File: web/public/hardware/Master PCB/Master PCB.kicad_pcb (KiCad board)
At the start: 2 copper layers, 100 x 100 mm, 98 parts, among them J1 Rows 0-15, J10 LDR2, J11 LDR3, J12 LDR4, J13 SWD Conn, J14 LED Conn, J15 OLED1, J16 OLED2, J17 Relay Conn, J2 Cols 0-21, J3 Cols 22-31, J4 5V_IN, J5 LED1, J6 LED2, J7 LED3, J8 LED4, J9 LDR1, Q1 2N7000, Q2 2N7000, Q3 2N7000, Q4 2N7000, SW1 nRST, SW2 Menu Encoder, U1 STM32U585VITx, U2 M95P32-IXMNT, U3 TLV62568DBV, U4 LM339, U5 MAX7375AXR805, U6 USBLC6-4SC6, U7 USBLC6-2SC6, U8 USBLC6-2SC6

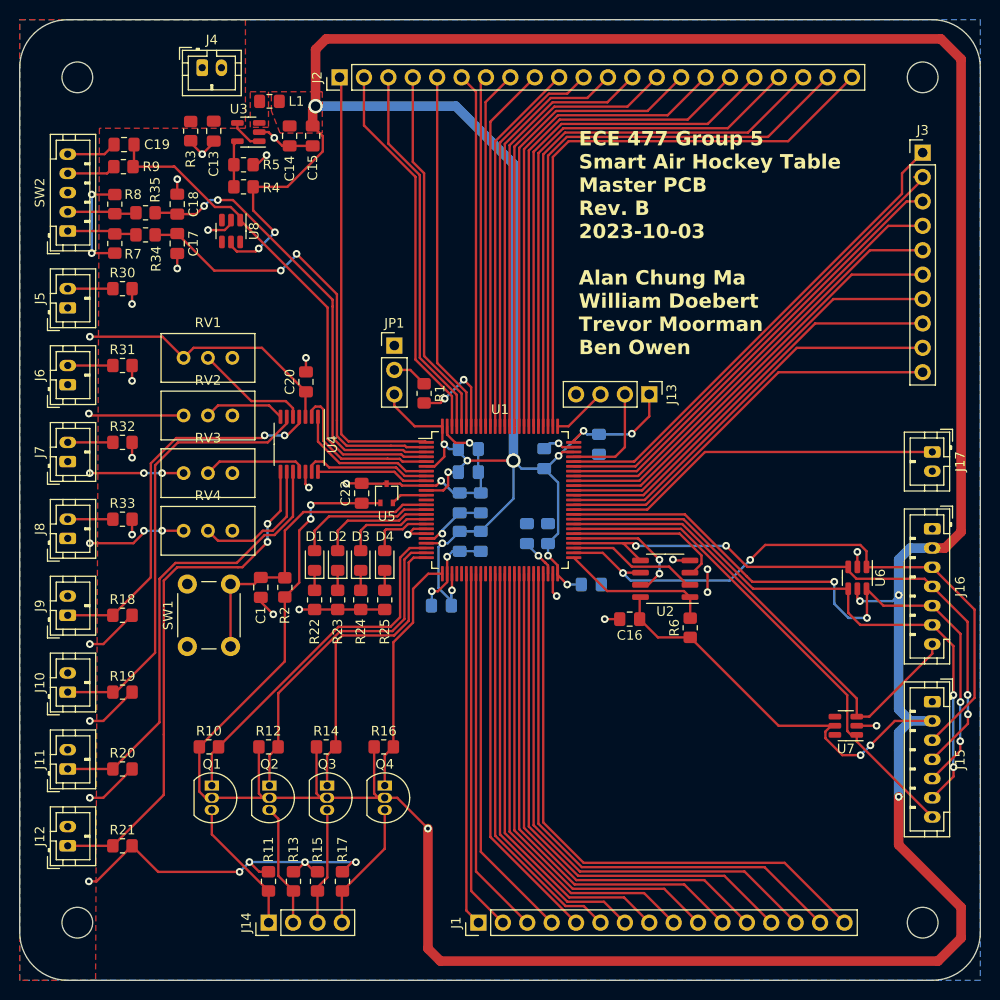
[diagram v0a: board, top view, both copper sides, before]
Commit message: Add labels, replace inductor, update routing
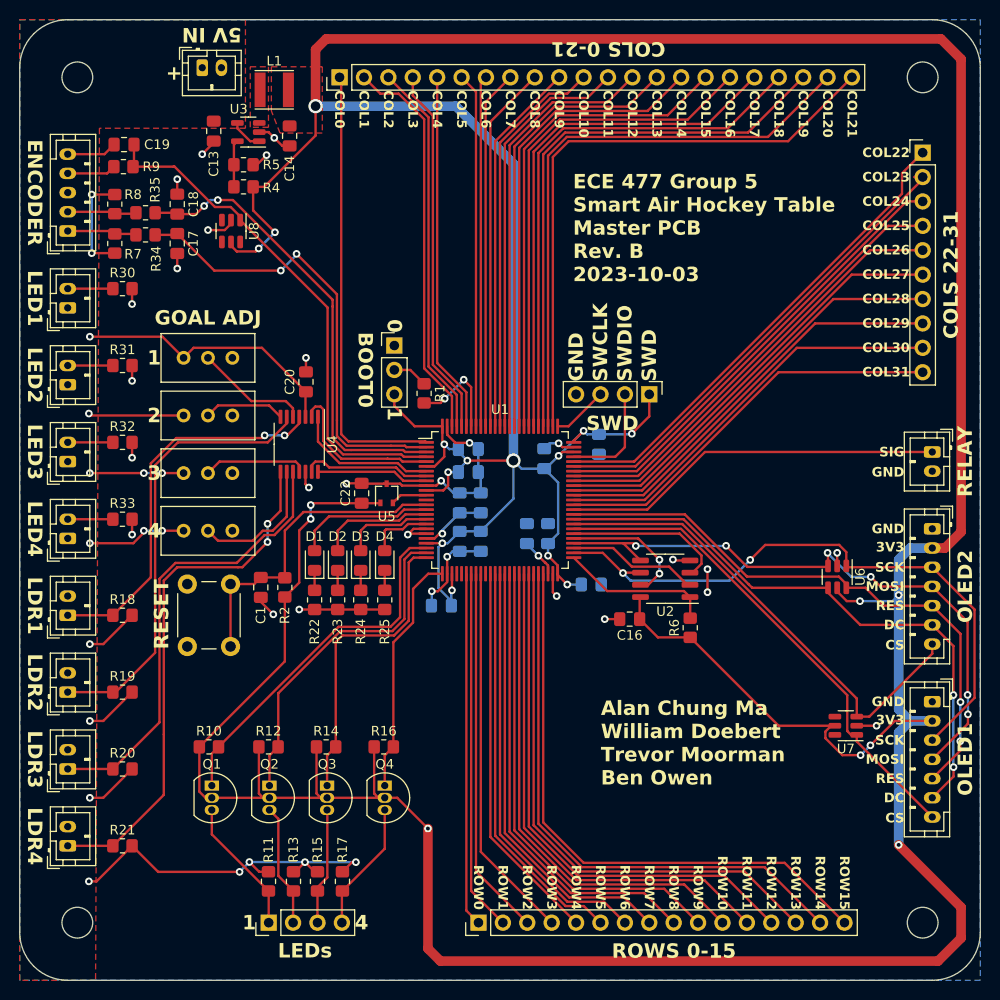
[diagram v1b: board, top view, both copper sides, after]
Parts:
- removed C15: 10uF, Capacitor_SMD:C_0805_2012Metric_Pad1.18x1.45mm_HandSolder
- removed R3: 499K, Resistor_SMD:R_0805_2012Metric_Pad1.20x1.40mm_HandSolder
- L1: footprint Inductor_SMD:L_0805_2012Metric_Pad1.15x1.40mm_HandSolder -> Inductor_SMD_Other:L_4.0x4.0_H1.8
- moved U6 2.10 mm to (185.1, 108.0)
- moved L1 1.30 mm to (126.5, 57.3)
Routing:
- net /OLEDRES: track 67.8 -> 61.9 mm, vias 4 -> 2
- net GND: track 97.7 -> 93.2 mm
- net /SPI2MOSI: track 63.0 -> 64.9 mm, vias 4 -> 6
- net /OLEDDC: track 63.2 -> 62.0 mm
- net /COL1: track 40.1 -> 41.2 mm
- net +3V3: track 550.8 -> 550.3 mm
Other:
- board text added: "+"
- board text added: "0"
- board text added: "1"
- board text added: "2"
- board text added: "3"
- board text added: "3V3"
- board text added: "4"
- board text added: "5V IN"
- board text added: "Alan Chung Ma William Doebert Trevor Moorman Ben Owen"
- board text added: "BOOT0"
- board text added: "COL0"
- board text added: "COL1"
- board text added: "COL10"
- board text added: "COL11"
- board text added: "COL12"
- board text added: "COL13"
- board text added: "COL14"
- board text added: "COL15"
- board text added: "COL16"
- board text added: "COL17"
- board text added: "COL18"
- board text added: "COL19"
- board text added: "COL2"
- board text added: "COL20"
- board text added: "COL21"
- board text added: "COL22"
- board text added: "COL23"
- board text added: "COL24"
- board text added: "COL25"
- board text added: "COL26"
- board text added: "COL27"
- board text added: "COL28"
- board text added: "COL29"
- board text added: "COL3"
- board text added: "COL30"
- board text added: "COL31"
- board text added: "COL4"
- board text added: "COL5"
- board text added: "COL6"
- board text added: "COL7"
- board text added: "COL8"
- board text added: "COL9"
- board text added: "COLS 0-21"
- board text added: "COLS 22-31"
- board text added: "CS"
- board text added: "DC"
- board text added: "ECE 477 Group 5 Smart Air Hockey Table Master PCB Rev. B 2023-10-03"
- board text added: "ENCODER"
- board text added: "GND"
- board text added: "GOAL ADJ"
- board text added: "LDR1"
- board text added: "LDR2"
- board text added: "LDR3"
- board text added: "LDR4"
- board text added: "LED1"
- board text added: "LED2"
- board text added: "LED3"
- board text added: "LED4"
- board text added: "LEDs"
- board text added: "MOSI"
- board text added: "OLED1"
- board text added: "OLED2"
- board text added: "RELAY"
- board text added: "RES"
- board text added: "RESET"
- board text added: "ROW0"
- board text added: "ROW1"
- board text added: "ROW10"
- board text added: "ROW11"
- board text added: "ROW12"
- board text added: "ROW13"
- board text added: "ROW14"
- board text added: "ROW15"
- board text added: "ROW2"
- board text added: "ROW3"
- board text added: "ROW4"
- board text added: "ROW5"
- board text added: "ROW6"
- board text added: "ROW7"
- board text added: "ROW8"
- board text added: "ROW9"
- board text added: "ROWS 0-15"
- board text added: "SCK"
- board text added: "SIG"
- board text added: "SWCLK"
- board text added: "SWD"
- board text added: "SWDIO"
- board text removed: "ECE 477 Group 5 Smart Air Hockey Table Master PCB Rev. B 2023-10-03 Alan Chung Ma William Doebert Trevor Moorman Ben Owen"

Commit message: Update labels
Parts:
- added D5: GRN, LED_SMD:LED_0805_2012Metric_Pad1.15x1.40mm_HandSolder, F.Cu at (113.7, 141.7)
- added D6: GRN, LED_SMD:LED_0805_2012Metric_Pad1.15x1.40mm_HandSolder, F.Cu at (117.3, 141.7)
- added R26: 100, Resistor_SMD:R_0805_2012Metric_Pad1.20x1.40mm_HandSolder, F.Cu at (117.3, 145.8)
- added R3: 100, Resistor_SMD:R_0805_2012Metric_Pad1.20x1.40mm_HandSolder, F.Cu at (113.7, 145.8)
- moved R35 5.59 mm to (117.2, 73.9)
- moved C19 5.59 mm to (115.0, 66.8)
- moved R34 5.59 mm to (117.2, 76.2)
- moved R9 5.59 mm to (114.9, 69.1)
- moved C17 5.59 mm to (120.5, 77.1)
- moved C18 5.59 mm to (120.5, 73.0)
- moved R7 5.59 mm to (114.0, 77.1)
- moved R8 5.59 mm to (114.0, 73.0)
- moved U8 5.59 mm to (126.1, 75.8)
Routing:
- net +3V3: track 550.3 -> 562.1 mm, vias 22 -> 24
- net +5V: track 128.1 -> 136.1 mm, vias 18 -> 19
- net /Menu Encoder/ENCODER_A: track 47.9 -> 41.4 mm
- net /Menu Encoder/ENCODER_B: track 48.2 -> 42.0 mm
- net Net-(SW2-A): track 7.27 -> 13.4 mm
- net Net-(SW2-B): track 7.22 -> 13.2 mm
- net /Menu Encoder/ENCODER_SW: track 53.5 -> 48.0 mm
- net Net-(SW2-S1): track 5.09 -> 10.2 mm
- net Net-(D6-K): track 0.00 -> 2.08 mm
- net Net-(D5-K): track 0.00 -> 2.08 mm
- net GND: track 93.2 -> 93.5 mm, vias 28 -> 30
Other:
- board text added: "5V"
- board text added: "A"
- board text added: "Alan Chung Ma William Dobert Trevor Moorman Ben Owen"
- board text added: "B"
- board text added: "ECE 477 Group 5 Smart Air Hockey Table Master PCB Rev. B 2023-10-04"
- board text added: "SW"
- board text removed: "Alan Chung Ma William Doebert Trevor Moorman Ben Owen"
- board text removed: "ECE 477 Group 5 Smart Air Hockey Table Master PCB Rev. B 2023-10-03"

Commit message: Fix vias
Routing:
- net /COL23: track 49.8 -> 48.9 mm
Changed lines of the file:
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@@
   (segment (start 124.598175 70.801825) (end 124.598175 67.698175) (width 0.25) (layer "F.Cu") (net 4))
   (via (at 124.598175 70.801825) (size 0.8) (drill 0.4) (layers "F.Cu" "B.Cu") (net 4))
-  (via (at 142.5 134.2) (size 0.8) (drill 0.4) (layers "F.Cu" "B.Cu") (net 4))
   (via (at 157 108.8) (size 0.8) (drill 0.4) (layers "F.Cu" "B.Cu") (net 4))
   (via (at 155 105.8) (size 0.8) (drill 0.4) (layers "F.Cu" "B.Cu") (net 4))
   (via (at 191.5 109.9) (size 0.8) (drill 0.4) (layers "F.Cu" "B.Cu") (net 4))
+  (via (at 191.5 135.9) (size 1.5) (drill 1) (layers "F.Cu" "B.Cu") (net 4))
   (via (at 163.7245 93.1) (size 0.8) (drill 0.4) (layers "F.Cu" "B.Cu") (net 4))
+  (via (at 142.5 134.2) (size 1.5) (drill 1) (layers "F.Cu" "B.Cu") (net 4))
   (via (at 156.1 95.4) (size 0.8) (drill 0.4) (layers "F.Cu" "B.Cu") (net 4))
-  (via (at 191.5 135.9) (size 0.8) (drill 0.4) (layers "F.Cu" "B.Cu") (net 4))
   (via (at 187.4755 110.526976) (size 0.8) (drill 0.4) (layers "F.Cu" "B.Cu") (net 4))
   (via (at 119.2 137.987799) (size 0.8) (drill 0.4) (layers "F.Cu" "B.Cu") (net 4))
@@
   (segment (start 164.106396 96.5) (end 157.675 96.5) (width 0.25) (layer "F.Cu") (net 33))
   (segment (start 194 66.606396) (end 194 66.38) (width 0.25) (layer "F.Cu") (net 33))
-  (segment (start 194 66.38) (end 193.12 66.38) (width 0.25) (layer "F.Cu") (net 33))
   (segment (start 164.106396 96.5) (end 194 66.606396) (width 0.25) (layer "F.Cu") (net 33))
   (segment (start 192.322792 68.92) (end 194 68.92) (width 0.25) (layer "F.Cu") (net 34))
@@
   (segment (start 168.972792 102.5) (end 187.1375 120.664708) (width 0.25) (layer "F.Cu") (net 46))
   (segment (start 188.45 122.55) (end 195 116) (width 0.25) (layer "F.Cu") (net 46))
-  (segment (start 194.6875 115) (end 195 115) (width 0.25) (layer "F.Cu") (net 46))
   (segment (start 125.5 93.2755) (end 125.2255 93.55) (width 0.25) (layer "F.Cu") (net 47))
   (segment (start 125.2255 93.55) (end 116.288299 93.55) (width 0.25) (layer "F.Cu") (net 47))
